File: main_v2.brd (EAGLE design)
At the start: 78.1 x 39.4 mm, 33 parts, among them IC1 MAX6921, IC2 MAX6921, IC3 MC33063, IC4 LD33V05T, IC5 TDA7052A

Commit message: Pracical modifications
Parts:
- removed SJ1, SJ3, SJ4, SJ6: (no value), jumper:SJ
- removed SJ2: (no value), jumper:SJ_2
- moved R1 1.00 mm to (70.2, 9.84)
- moved C4 1.00 mm to (72.7, 11.7)
- moved C5 1.00 mm to (71.4, 29.5)
- moved IC5 1.00 mm to (70.8, 20.6)
- moved R12 1.00 mm to (67.0, 9.84)
- moved R11 1.00 mm to (67.0, 30.8)
- moved IC1 0.63 mm to (39.4, 10.8), turned to 90 degrees
- turned IC2 to 90 degrees
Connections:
- removed net HT+1: H1.1, H2.1, SJ2.3, SJ3.2
- removed net HT+4: H3.1, H4.1, SJ3.1
- removed net HT-1: H1.2, SJ2.1, SJ4.2
- removed net HT-2: H2.2, SJ1.1, SJ4.1
- removed net HT-3: H3.2, SJ1.2, SJ6.2
- removed net HT-4: H4.2, R11.1, SJ6.1
- new net HT+: H1.1, H2.1, H3.1, H4.1, R11.1
- new net HT-: H1.2, H2.2, H3.2, H4.2, R12.1
- new net N$14: IC1.4
- new net N$15: IC1.5
- new net N$16: IC1.6
- new net N$17: IC1.7
- new net N$18: IC1.8
- new net N$19: IC1.9
- new net N$20: IC1.10
- new net N$21: IC1.11
- new net N$22: IC1.12
- new net N$23: IC1.17
- new net N$24: IC1.18
- new net N$25: IC1.19
- new net N$26: IC1.20
- new net N$27: IC1.21
- new net N$28: IC1.22
- new net N$29: IC1.23
- new net N$30: IC1.24
- new net N$31: IC1.25
- new net N$32: IC1.26
- new net N$33: IC2.26
- new net N$34: IC2.25
- new net N$35: IC2.24
- new net N$36: IC2.23
- new net N$37: IC2.22
- new net N$38: IC2.21
- new net N$39: IC2.20
- new net N$40: IC2.19
- new net N$41: IC2.18
- new net N$42: IC2.17
- new net N$43: IC2.12
- new net N$44: IC2.11
- new net N$45: IC2.10
- new net N$46: IC2.9
- new net N$47: IC2.8
- new net N$48: IC2.7
- new net N$49: IC2.6
- new net N$50: IC2.5
- new net N$51: IC2.4
- new net N$52: IC2.3
- net N$13: now also IC1.3; no longer R12.1, SJ2.2
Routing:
- net VBB: track 80.7 -> 42.2 mm
- net HT+: track 0.00 -> 38.0 mm
- net HT-: track 0.00 -> 37.7 mm
- net HT-1: track 15.0 -> 0.00 mm
- net HT-2: track 11.0 -> 0.00 mm
- net N$13: track 3.07 -> 0.00 mm
- net HT-3: track 3.05 -> 0.00 mm
- net HT+1: track 2.65 -> 0.00 mm
- net VCC: track 114.1 -> 113.0 mm
- net GND: track 149.2 -> 148.6 mm

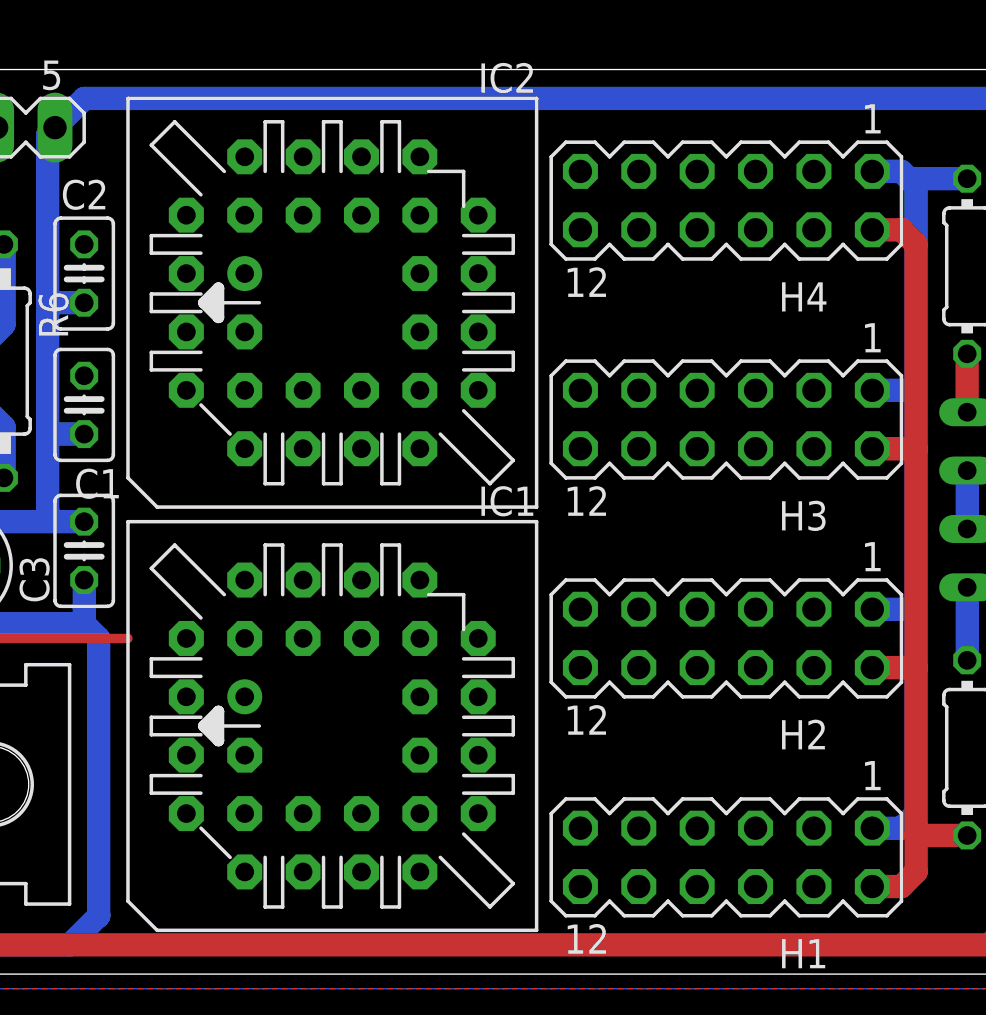
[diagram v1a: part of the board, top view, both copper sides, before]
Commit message: Try wiring a few routes
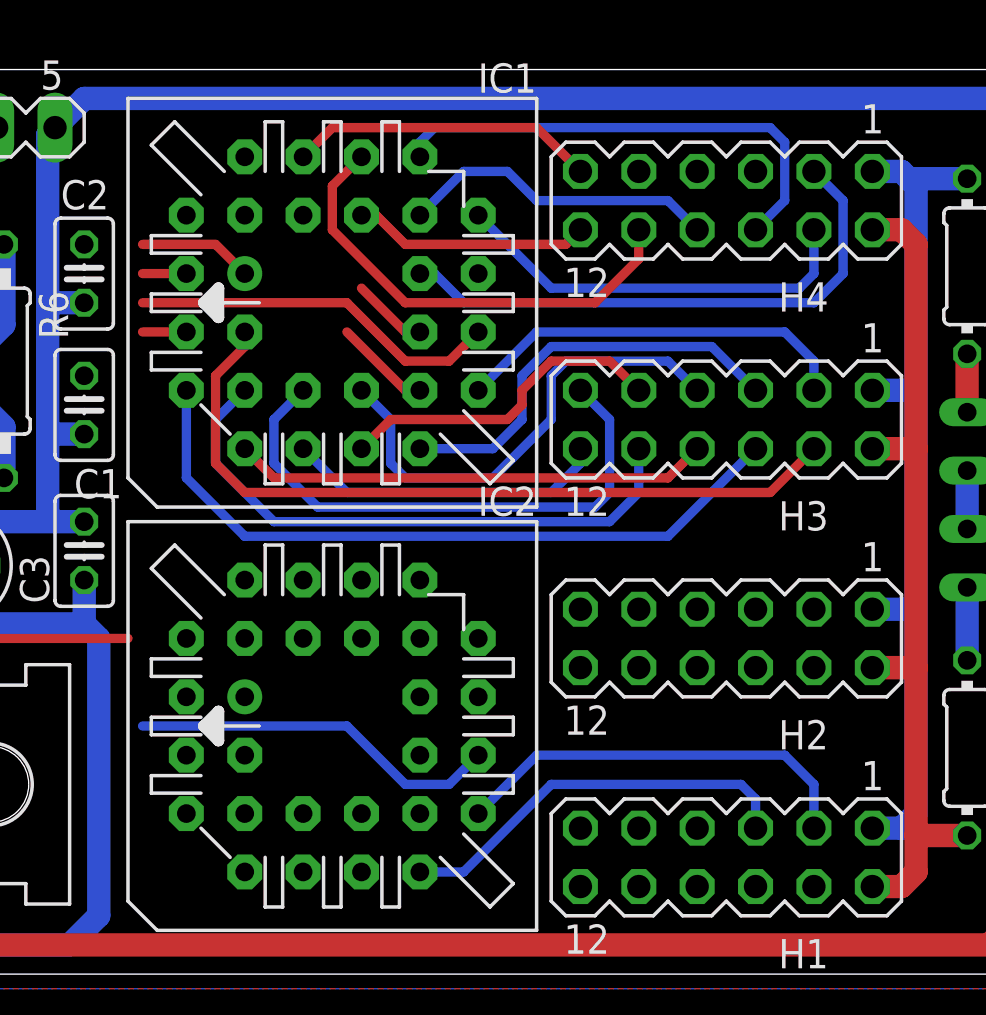
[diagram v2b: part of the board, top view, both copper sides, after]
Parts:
- moved IC1 18.4 mm to (39.4, 29.2)
- moved IC2 18.4 mm to (39.4, 10.8)
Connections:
- removed net N$13: IC1.3
- removed net N$14: IC1.4
- removed net N$15: IC1.5
- removed net N$16: IC1.6
- removed net N$17: IC1.7
- removed net N$18: IC1.8
- removed net N$19: IC1.9
- removed net N$20: IC1.10
- removed net N$21: IC1.11
- removed net N$22: IC1.12
- removed net N$23: IC1.17
- removed net N$24: IC1.18
- removed net N$25: IC1.19
- removed net N$26: IC1.20
- removed net N$27: IC1.21
- removed net N$28: IC1.22
- removed net N$29: IC1.23
- removed net N$30: IC1.24
- removed net N$31: IC1.25
- removed net N$32: IC1.26
- removed net N$43: IC2.12
- removed net N$44: IC2.11
- net GATE1: now also IC2.12
- net GATE3: now also IC1.12
- net GATE4: now also IC1.17
- net OUT16: now also IC1.11
- net OUT17: now also IC1.10
- net OUT18: now also IC1.9
- net OUT19: now also IC1.8
- net OUT20: now also IC1.7
- net OUT21: now also IC1.6
- net OUT22: now also IC1.5
- net OUT23: now also IC1.4
- net OUT24: now also IC1.26
- net OUT25: now also IC1.25
- net OUT26: now also IC1.24
- net OUT27: now also IC1.23
- net OUT28: now also IC1.22
- net OUT29: now also IC1.21
- net OUT3: now also IC2.11
- net OUT30: now also IC1.20
- net OUT31: now also IC1.19
- net SPARE3: now also IC1.3
- net SPARE4: now also IC1.18
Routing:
- net SPARE3: track 0.00 -> 33.6 mm
- net GND: track 148.6 -> 181.0 mm
- net OUT23: track 0.00 -> 31.2 mm
- net OUT21: track 0.00 -> 25.6 mm
- net GATE4: track 0.00 -> 24.4 mm
- net OUT19: track 0.00 -> 24.3 mm
- net OUT31: track 0.00 -> 21.4 mm
- net OUT17: track 0.00 -> 21.0 mm
- net OUT22: track 0.00 -> 20.7 mm
- net OUT29: track 0.00 -> 20.4 mm
- net OUT16: track 0.00 -> 18.4 mm
- net SPARE4: track 0.00 -> 18.1 mm
- net GATE1: track 0.00 -> 18.1 mm
- net OUT3: track 0.00 -> 17.7 mm
- net GATE3: track 0.00 -> 17.5 mm
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
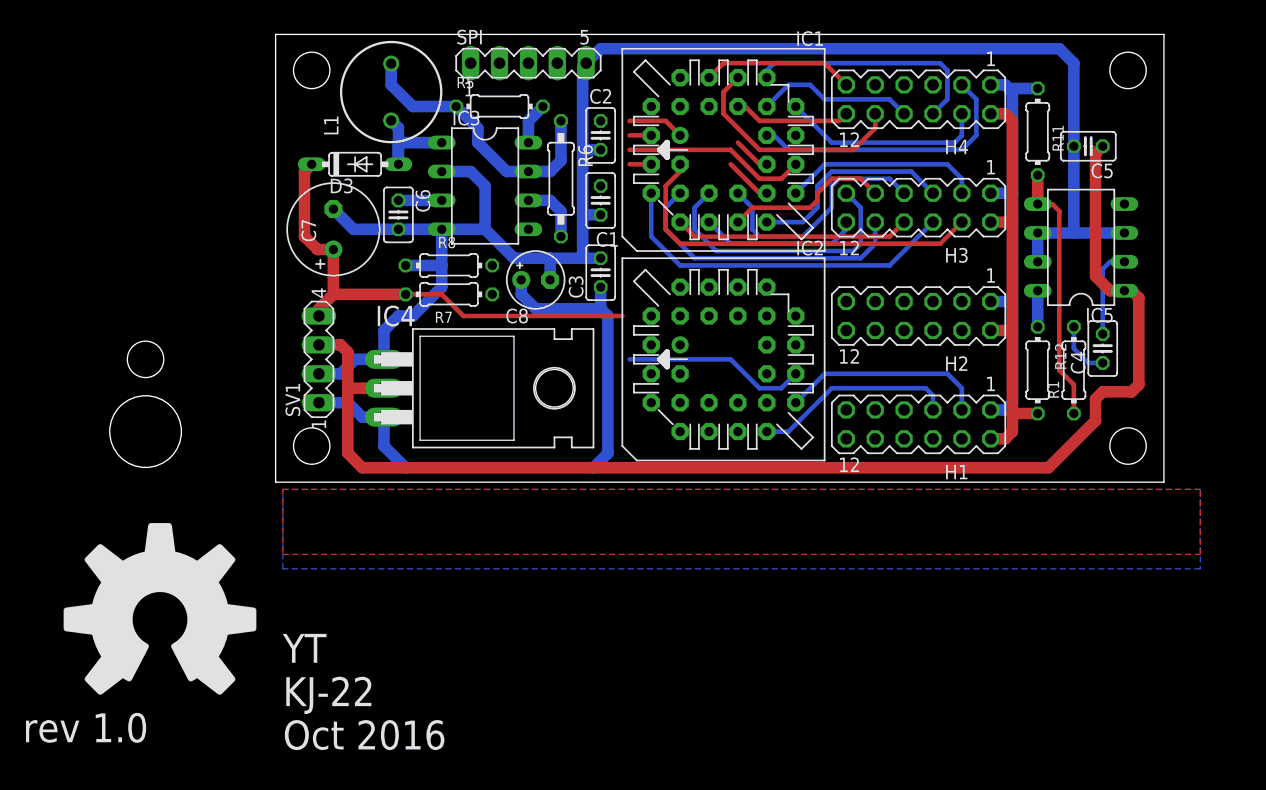
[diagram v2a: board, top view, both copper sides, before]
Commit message: Wire most of the board
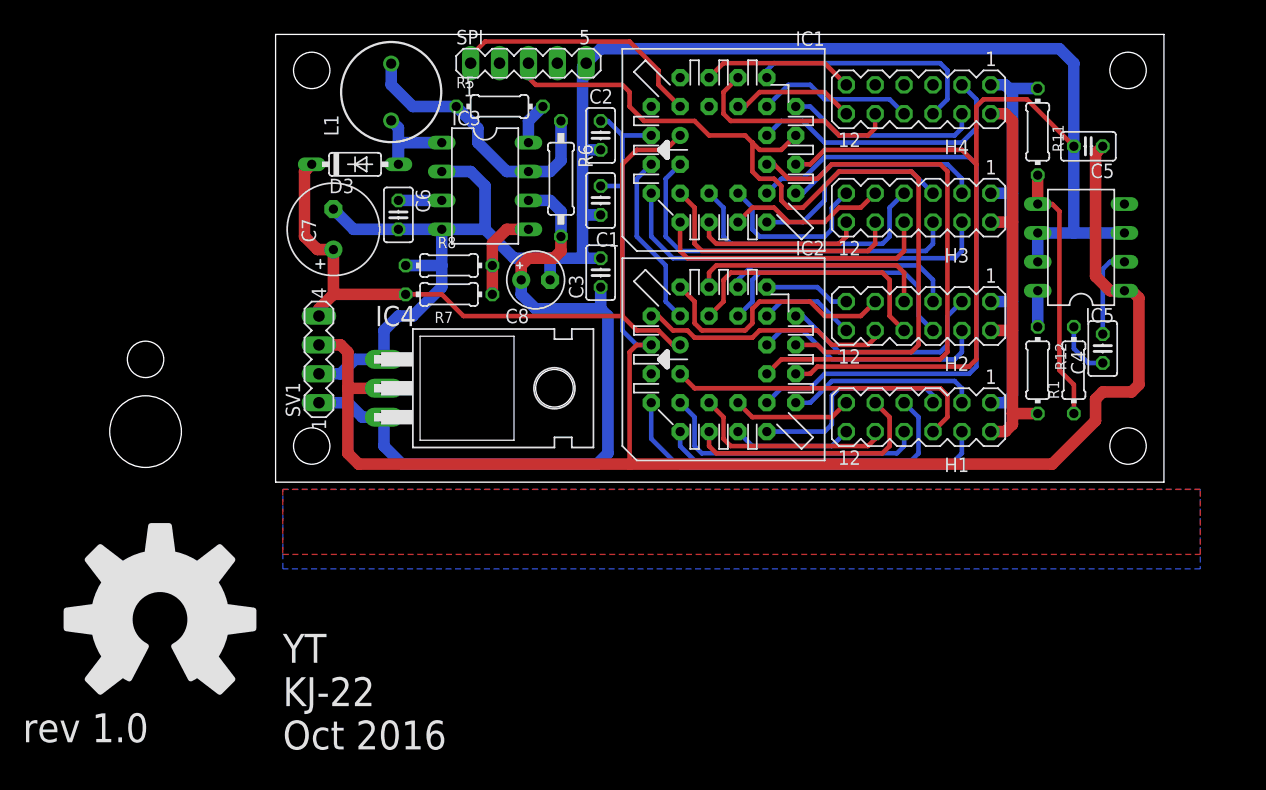
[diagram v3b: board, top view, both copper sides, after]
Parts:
- moved H1 0.63 mm to (56.5, 5.71)
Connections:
- removed net N$33: IC2.26
- removed net N$34: IC2.25
- removed net N$35: IC2.24
- removed net N$36: IC2.23
- removed net N$37: IC2.22
- removed net N$38: IC2.21
- removed net N$39: IC2.20
- removed net N$40: IC2.19
- removed net N$41: IC2.18
- removed net N$42: IC2.17
- removed net N$45: IC2.10
- removed net N$46: IC2.9
- removed net N$47: IC2.8
- removed net N$48: IC2.7
- removed net N$49: IC2.6
- removed net N$50: IC2.5
- removed net N$51: IC2.4
- removed net N$52: IC2.3
- net GATE2: now also IC2.18
- net OUT0: now also IC2.10
- net OUT1: now also IC2.7
- net OUT10: now also IC2.25
- net OUT11: now also IC2.19
- net OUT12: now also IC2.20
- net OUT13: now also IC2.26
- net OUT14: now also IC2.24
- net OUT15: now also IC2.22
- net OUT17: now also IC1.8; no longer IC1.10
- net OUT19: now also IC1.10; no longer IC1.8
- net OUT2: now also IC2.5
- net OUT23: now also IC1.3; no longer IC1.4
- net OUT4: now also IC2.9
- net OUT5: now also IC2.8
- net OUT6: now also IC2.6
- net OUT7: now also IC2.3
- net OUT8: now also IC2.21
- net OUT9: now also IC2.23
- net SPARE1: now also IC2.4
- net SPARE2: now also IC2.17
- net SPARE3: now also IC1.4; no longer IC1.3
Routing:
- net N$4: track 0.00 -> 75.4 mm
- net N$3: track 4.23 -> 57.5 mm
- net SCK: track 3.33 -> 49.7 mm
- net VCC: track 114.9 -> 151.8 mm
- net SPARE1: track 0.00 -> 34.0 mm
- net GND: track 181.0 -> 214.7 mm
- net OUT2: track 0.00 -> 28.0 mm
- net OUT7: track 0.00 -> 28.0 mm
- net OUT6: track 0.00 -> 24.5 mm
- net OUT14: track 0.00 -> 23.8 mm
- net OUT15: track 0.00 -> 23.4 mm
- net MOSI: track 0.00 -> 22.7 mm
- net OUT10: track 0.00 -> 22.7 mm
- net OUT13: track 0.00 -> 22.2 mm
- net OUT1: track 0.00 -> 22.0 mm
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
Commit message: More work on the board
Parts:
- moved C1 6.35 mm to (28.6, 18.4), turned to 90 degrees
- moved C3 3.24 mm to (25.4, 17.8)
- moved C8 1.91 mm to (21.0, 17.8)
- moved R7 1.90 mm to (13.3, 16.5)
- moved R8 1.90 mm to (13.3, 19.1)
- moved C2 1.27 mm to (28.6, 29.2)
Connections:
- net GATE4: now also IC1.25; no longer IC1.17
- net OUT24: now also IC1.23; no longer IC1.26
- net OUT25: now also IC1.21; no longer IC1.25
- net OUT26: now also IC1.22; no longer IC1.24
- net OUT27: now also IC1.19; no longer IC1.23
- net OUT28: now also IC1.20; no longer IC1.22
- net OUT29: now also IC1.18; no longer IC1.21
- net OUT30: now also IC1.17; no longer IC1.20
- net OUT31: now also IC1.24; no longer IC1.19
- net SPARE4: now also IC1.26; no longer IC1.18
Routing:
- net N$4: track 75.4 -> 44.2 mm
- net GND: track 214.7 -> 190.1 mm
- net OUT24: track 0.00 -> 22.3 mm
- net SPARE4: track 17.2 -> 37.1 mm
- net OUT25: track 0.00 -> 15.9 mm
- net OUT26: track 0.00 -> 13.4 mm
- net OUT29: track 19.4 -> 8.30 mm
- net MOSI: track 22.7 -> 15.1 mm
- net OUT27: track 13.4 -> 7.77 mm
- net +5V: track 65.2 -> 68.4 mm
- net OUT28: track 10.8 -> 8.30 mm
- net OUT22: track 25.3 -> 22.9 mm
- net OUT21: track 23.3 -> 21.3 mm
- net GATE4: track 24.6 -> 26.5 mm
- net OUT20: track 15.1 -> 13.5 mm
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
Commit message: Nearly there
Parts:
- moved H3 0.64 mm to (56.5, 24.8)
- moved H1 0.63 mm to (56.5, 6.35)
- moved H2 0.63 mm to (56.5, 15.2)
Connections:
- net N$3: now also SPI.2; no longer SPI.4
- net SCK: now also SPI.4; no longer SPI.2
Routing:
- net SCK: track 49.0 -> 72.2 mm
- net OUT7: track 28.0 -> 29.7 mm
- net GATE2: track 19.2 -> 18.1 mm
- net N$3: track 56.8 -> 55.6 mm
- net OUT16: track 18.0 -> 17.0 mm
- net N$4: track 44.2 -> 43.3 mm
- net SPARE2: track 20.5 -> 19.7 mm
- net OUT9: track 20.7 -> 20.1 mm
- net OUT8: track 20.7 -> 20.1 mm
- net OUT19: track 14.9 -> 15.5 mm
- net OUT14: track 23.8 -> 23.2 mm
- net OUT1: track 22.0 -> 22.6 mm
- net GATE3: track 17.5 -> 16.8 mm
- net OUT15: track 23.4 -> 22.8 mm
- net HT-: track 37.0 -> 36.4 mm
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
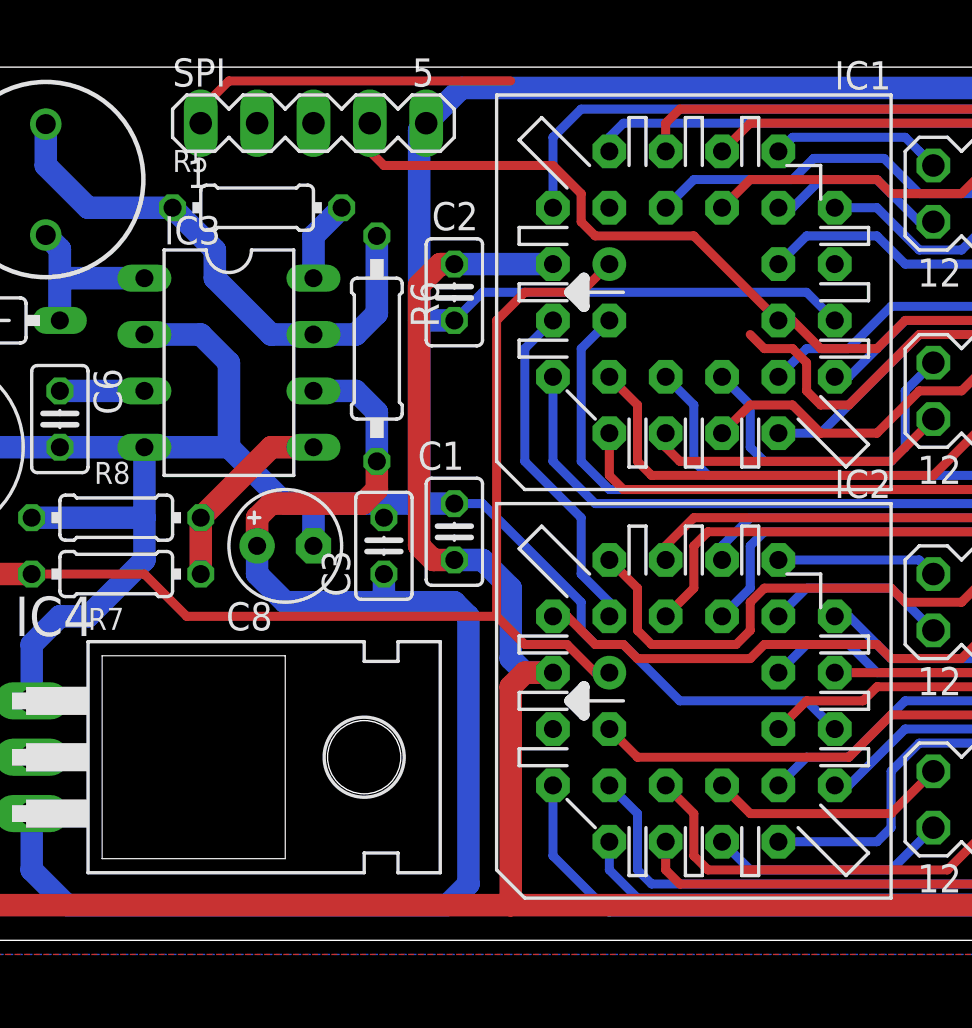
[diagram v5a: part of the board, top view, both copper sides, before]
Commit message: Try SPI header vertically
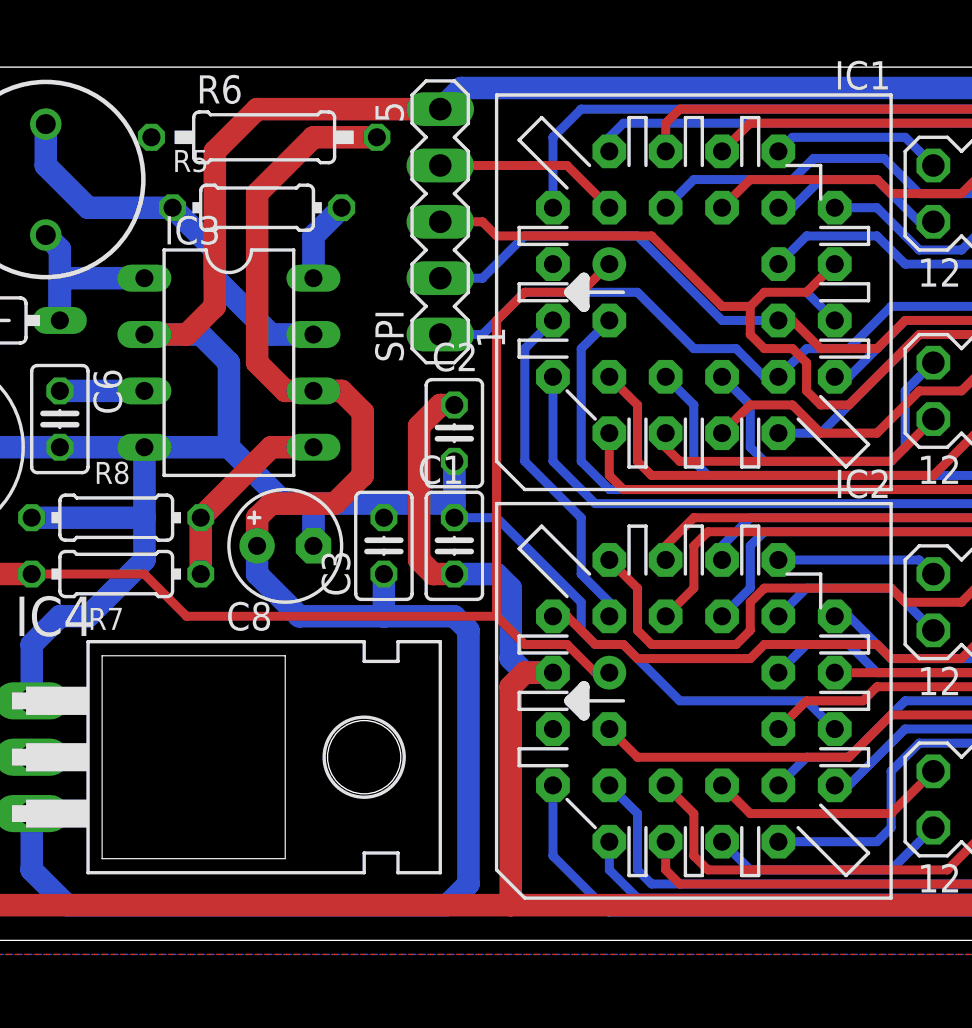
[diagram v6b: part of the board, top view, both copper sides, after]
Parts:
- moved R6 10.8 mm to (20.0, 36.2), turned to 0 degrees
- moved SPI 7.24 mm to (27.9, 32.4), turned to 90 degrees
- moved C2 6.35 mm to (28.6, 22.9)
- moved C1 0.63 mm to (28.6, 17.8)
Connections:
- net MOSI: now also SPI.4; no longer SPI.1
- net N$3: now also SPI.1; no longer SPI.2
- net SCK: now also SPI.2; no longer SPI.4
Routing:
- net N$4: track 43.3 -> 64.7 mm
- net N$3: track 55.6 -> 73.3 mm
- net +5V: track 68.4 -> 84.1 mm
- net GND: track 190.1 -> 177.7 mm
- net VCC: track 153.2 -> 142.7 mm
- net N$8: track 24.6 -> 17.8 mm
- net MOSI: track 15.1 -> 8.41 mm
- net SCK: track 72.2 -> 66.2 mm

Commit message: Well, its finished
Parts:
- moved R6 10.8 mm to (25.1, 26.7), turned to 270 degrees
- moved C2 6.35 mm to (28.6, 29.2)
- moved SPI 5.85 mm to (23.5, 36.2), turned to 180 degrees
- moved C1 0.63 mm to (28.6, 18.4)
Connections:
- net MOSI: now also SPI.1; no longer SPI.4
- net N$3: now also SPI.2; no longer SPI.1
- net SCK: now also SPI.4; no longer SPI.2
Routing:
- net GND: track 177.7 -> 203.6 mm
- net +5V: track 84.1 -> 68.0 mm
- net N$4: track 64.7 -> 76.2 mm
- net VCC: track 142.7 -> 152.3 mm
- net SCK: track 66.2 -> 75.0 mm
- net N$3: track 73.3 -> 81.1 mm
- net N$8: track 17.8 -> 24.6 mm
- removed copper zone on layer 1, net GND
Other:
- board size 78.1 x 39.4 mm -> 76.8 x 39.4 mm
- board text added: "JLCJLCJLCJLC"
- board text added: "VBB VCC GND IN"
- board text added: "YT KJ-22 Apr 2021"
- board text added: "rev 2.0"
- board text removed: "YT KJ-22 Oct 2016"
- board text removed: "rev 1.0"
